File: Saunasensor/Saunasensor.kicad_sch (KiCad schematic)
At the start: 0 parts

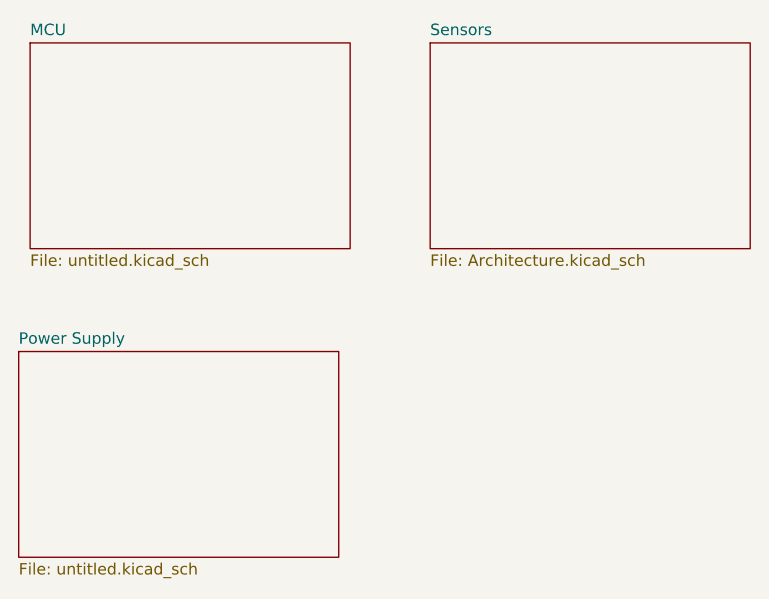
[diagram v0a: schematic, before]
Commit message: Schematic work
* added sensors
* added power supply
* added MCU
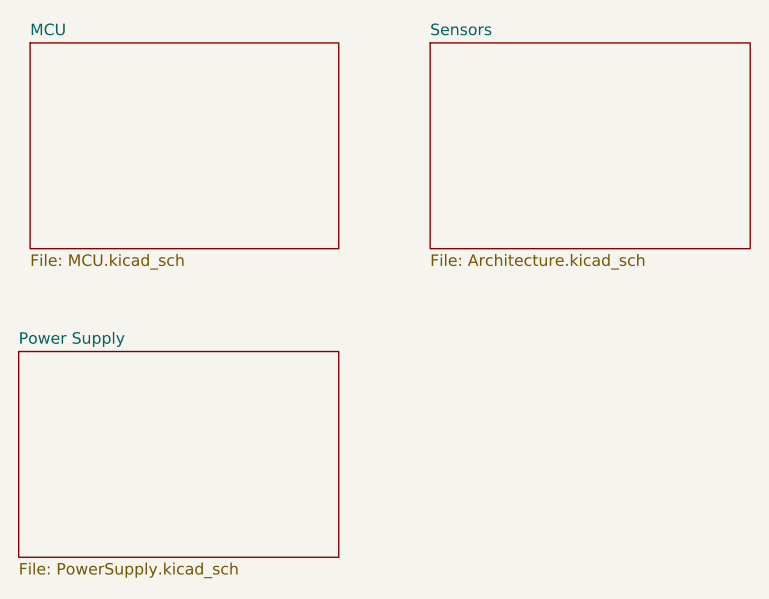
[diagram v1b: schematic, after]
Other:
- sheet MCU: file untitled.kicad_sch -> MCU.kicad_sch
- sheet Power Supply: file untitled.kicad_sch -> PowerSupply.kicad_sch
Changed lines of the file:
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@@
 			)
 		)
-		(property "Sheetfile" "untitled.kicad_sch"
+		(property "Sheetfile" "PowerSupply.kicad_sch"
 			(at 57.15 99.6446 0)
 			(effects
@@
 				(path "/0be96024-9d02-430f-aeb4-07f5cd93af40"
 					(page "3")
+				)
+			)
+		)
+	)
+	(sheet
+		(at 58.42 41.91)
+		(size 34.29 22.86)
+		(fields_autoplaced yes)
+		(stroke
+			(width 0.1524)
+			(type solid)
+		)
+		(fill
+			(color 0 0 0 0.0000)
+		)
+		(property "Sheetname" "MCU"
+			(at 58.42 41.1984 0)
+			(effects
+				(font
+					(size 1.27 1.27)
+				)
+				(justify left bottom)
+			)
+		)
+		(property "Sheetfile" "MCU.kicad_sch"
+			(at 58.42 65.3546 0)
+			(effects
+				(font
+					(size 1.27 1.27)
+				)
+				(justify left top)
+			)
+		)
+		(instances
+			(project "Saunasensor"
+				(path "/0be96024-9d02-430f-aeb4-07f5cd93af40"
+					(page "4")
 				)
 			)
@@
 				)
 			)
-		)
-	)
-	(sheet
-		(at 58.42 41.91)
-		(size 35.56 22.86)
-		(fields_autoplaced yes)
-		(stroke
-			(width 0.1524)
-			(type solid)
-		)
-		(fill
-			(color 0 0 0 0.0000)
-		)
-		(property "Sheetname" "MCU"
-			(at 58.42 41.1984 0)
-			(effects
-				(font
-					(size 1.27 1.27)
-				)
-				(justify left bottom)
-			)
-		)
-		(property "Sheetfile" "untitled.kicad_sch"
-			(at 58.42 65.3546 0)
-			(effects
-				(font
-					(size 1.27 1.27)
-				)
-				(justify left top)
-			)
-		)
-		(instances
-			(project "Saunasensor"
-				(path "/0be96024-9d02-430f-aeb4-07f5cd93af40"
-					(page "4")
-				)
-			)
